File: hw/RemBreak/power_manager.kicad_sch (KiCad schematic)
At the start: 20 parts, among them IC1 LTC2943IDD#TRPBF, J10 Screw_Terminal_01x02, J11 Conn_01x03, Q4 BC337, Q5 BC847, U5 INA219BxDCN, U7 MAX40200AUK

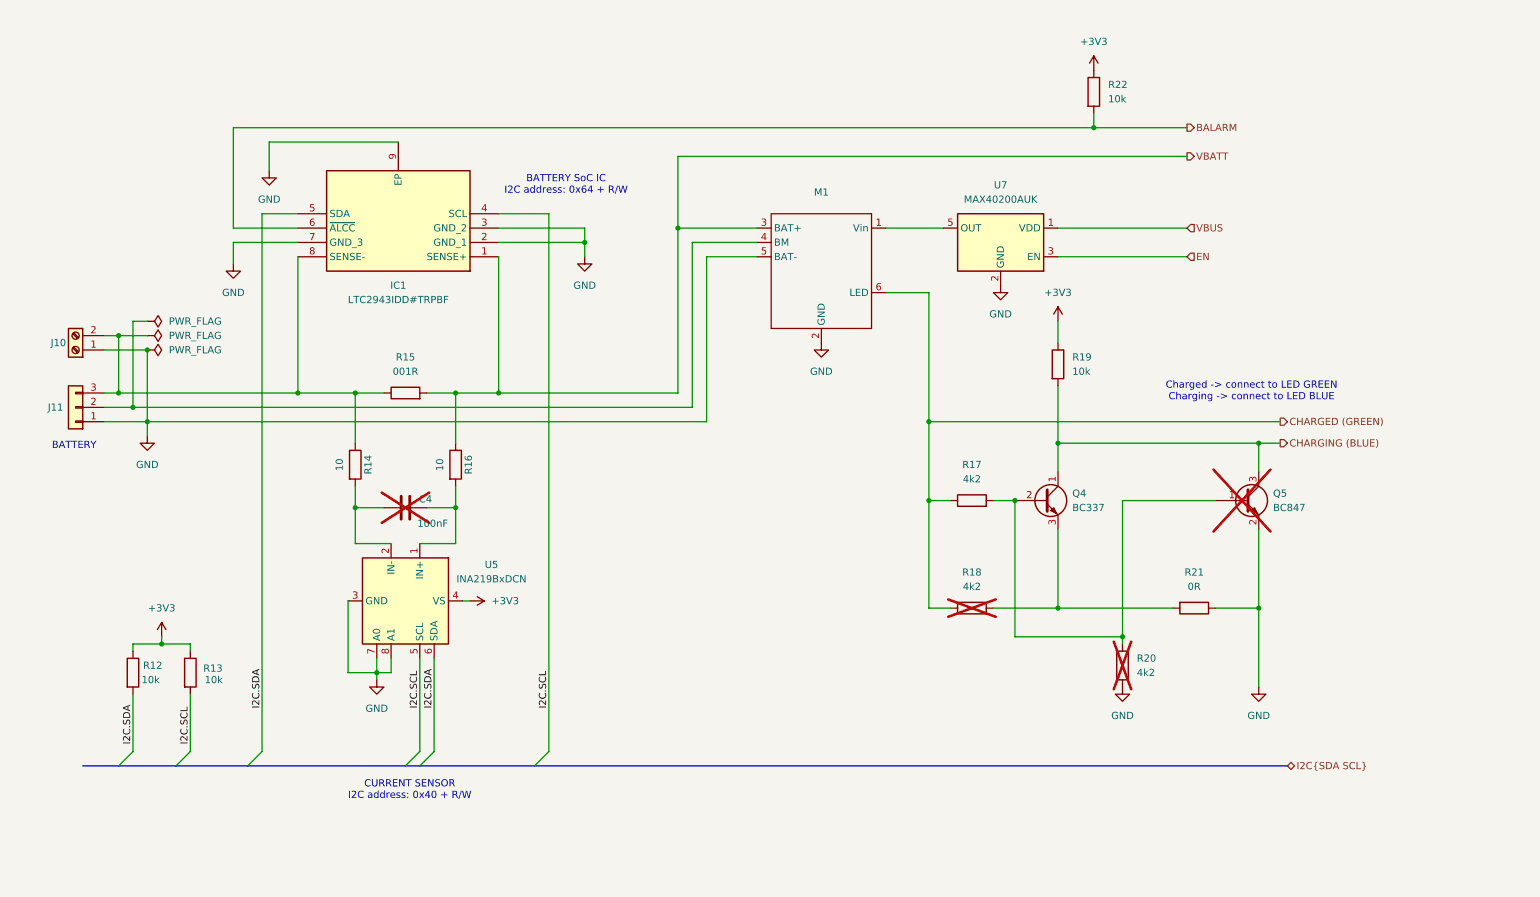
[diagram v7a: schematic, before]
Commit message: regenerated anotations and used battery connector with grounding
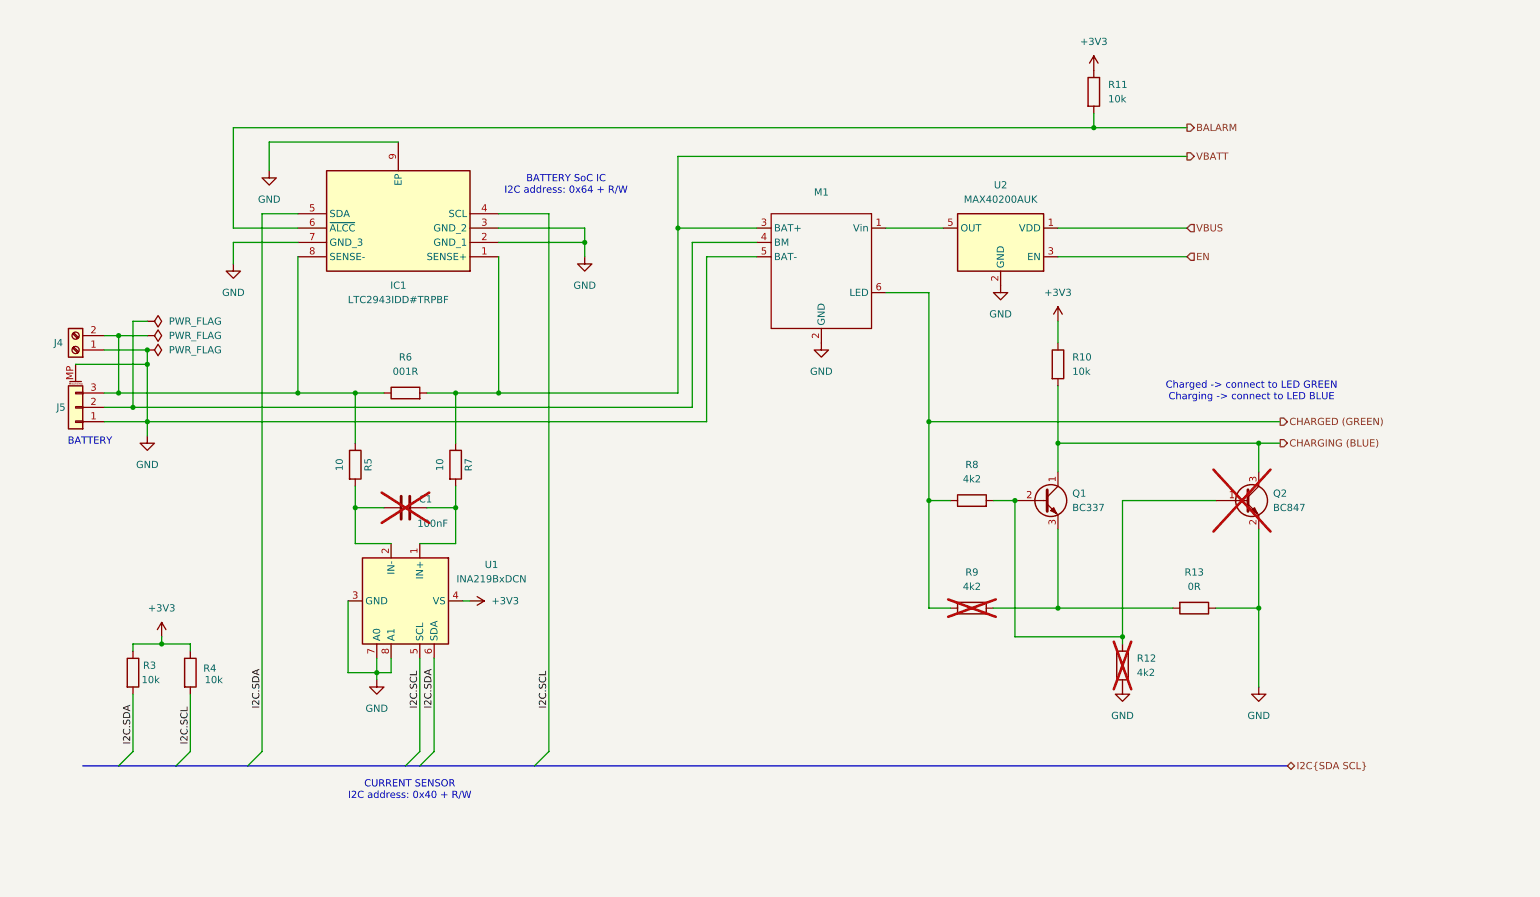
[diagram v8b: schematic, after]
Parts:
- removed J11: Conn_01x03, Connector_JST:JST_XH_S3B-XH-SM4-TB_1x03-1MP_P2.50mm_Horizontal, symbol Connector_Generic:Conn_01x03
- added J5: Conn_01x03_MountingPin, Connector_JST:JST_XH_S3B-XH-SM4-TB_1x03-1MP_P2.50mm_Horizontal, symbol Connector_Generic_MountingPin:Conn_01x03_MountingPin
- renumbered C4 to C1, J10 to J4, Q4 to Q1, Q5 to Q2, R19 to R10, R22 to R11, R20 to R12, R21 to R13, R12 to R3, R13 to R4, R14 to R5, R15 to R6, R16 to R7, R17 to R8, R18 to R9, U5 to U1, U7 to U2
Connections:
- net GND: now also J5.1 (Pin_1), J5.MP (MountPin)
- net at IC1.8 (SENSE-), J4.2 (Pin_2), R5.1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: now also J5.3 (Pin_3)
- net at M1.4 (BM): now also J5.2 (Pin_2)
